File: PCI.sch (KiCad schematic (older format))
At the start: 67 parts

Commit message: workworkwork
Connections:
- net N12_PCI renamed N12V_PCI
- net P12_PCI renamed P12V_PCI
- removed net P3V3_PCI: C37.1, C38.1, C41.1, C42.1, C45.1, C46.1, C49.1, C50.1, PCI0.A10, PCI0.A16, PCI0.A21, PCI0.A27, PCI0.A33, PCI0.A39, PCI0.A45, PCI0.A53, PCI0.A59, PCI0.B19, PCI0.B25, PCI0.B31, PCI0.B36, PCI0.B41, PCI0.B43, PCI0.B54, PCI0.B59, PCI1.A10, PCI1.A16, PCI1.A21, PCI1.A27, PCI1.A33, PCI1.A39, PCI1.A45, PCI1.A53, PCI1.A59, PCI1.B19, PCI1.B25, PCI1.B31, PCI1.B36, PCI1.B41, PCI1.B43, PCI1.B54, PCI1.B59, PCI2.A10, PCI2.A16, PCI2.A21, PCI2.A27, PCI2.A33, PCI2.A39, PCI2.A45, PCI2.A53, PCI2.A59, PCI2.B19, PCI2.B25, PCI2.B31, PCI2.B36, PCI2.B41, PCI2.B43, PCI2.B54, PCI2.B59, PCI3.A10, PCI3.A16, PCI3.A21, PCI3.A27, PCI3.A33, PCI3.A39, PCI3.A45, PCI3.A53, PCI3.A59, PCI3.B19, PCI3.B25, PCI3.B31, PCI3.B36, PCI3.B41, PCI3.B43, PCI3.B54, PCI3.B59, R27.1, R28.1, R29.1, R30.1, R31.1, R32.1, R33.1, R34.1, R35.1, R36.1, R37.1, R38.1, R39.1, R40.1, R41.1, R42.1, R43.1, R44.1, R45.1, R46.1, R47.1, R48.1, R49.2
- net P3V3_PCI_AUX renamed P3V3_PCI_A
- net P3V3_PCI_A: now also C37.1, C38.1, C45.1, C46.1, PCI0.A10, PCI0.A16, PCI0.A21, PCI0.A27, PCI0.A33, PCI0.A39, PCI0.A45, PCI0.A53, PCI0.A59, PCI0.B19, PCI0.B25, PCI0.B31, PCI0.B36, PCI0.B41, PCI0.B43, PCI0.B54, PCI0.B59, PCI2.A10, PCI2.A16, PCI2.A21, PCI2.A27, PCI2.A33, PCI2.A39, PCI2.A45, PCI2.A53, PCI2.A59, PCI2.B19, PCI2.B25, PCI2.B31, PCI2.B36, PCI2.B41, PCI2.B43, PCI2.B54, PCI2.B59; no longer PCI1.A14, PCI3.A14
- net P5_PCI renamed P5V_PCI_A
- net P5V_PCI_A: no longer C40.1, C48.1, C72.1, C74.1, PCI1.A5, PCI1.A61, PCI1.A62, PCI1.A8, PCI1.B5, PCI1.B6, PCI1.B61, PCI1.B62, PCI3.A5, PCI3.A61, PCI3.A62, PCI3.A8, PCI3.B5, PCI3.B6, PCI3.B61, PCI3.B62
- new net P3V3_AUX: R39.1, R40.1, R41.1, R42.1, R43.1, R44.1, R45.1, R46.1, R47.1, R48.1, R49.2
- new net P3V3_BRIDGE: R27.1, R28.1, R29.1, R30.1, R31.1, R32.1, R33.1, R34.1, R35.1, R36.1, R37.1, R38.1
- new net P3V3_PCI_B: C41.1, C42.1, C49.1, C50.1, PCI1.A10, PCI1.A14, PCI1.A16, PCI1.A21, PCI1.A27, PCI1.A33, PCI1.A39, PCI1.A45, PCI1.A53, PCI1.A59, PCI1.B19, PCI1.B25, PCI1.B31, PCI1.B36, PCI1.B41, PCI1.B43, PCI1.B54, PCI1.B59, PCI3.A10, PCI3.A14, PCI3.A16, PCI3.A21, PCI3.A27, PCI3.A33, PCI3.A39, PCI3.A45, PCI3.A53, PCI3.A59, PCI3.B19, PCI3.B25, PCI3.B31, PCI3.B36, PCI3.B41, PCI3.B43, PCI3.B54, PCI3.B59
- new net P5V_PCI_B: C40.1, C48.1, C72.1, C74.1, PCI1.A5, PCI1.A61, PCI1.A62, PCI1.A8, PCI1.B5, PCI1.B6, PCI1.B61, PCI1.B62, PCI3.A5, PCI3.A61, PCI3.A62, PCI3.A8, PCI3.B5, PCI3.B6, PCI3.B61, PCI3.B62

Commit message: TODO: learn to write good commit messages
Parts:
- added C116, C117, C118, C119, C120, C121: 1u, IPC7351-Nominal:CAPC1005X55, symbol C-0402
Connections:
- net P3V3_BRIDGE: now also C116.2, C117.2, C118.2, C119.2, C120.2, C121.2
- net P3V3_PCI_A: now also C118.1, C120.1, C121.1
- net P3V3_PCI_B: now also C116.1, C117.1, C119.1

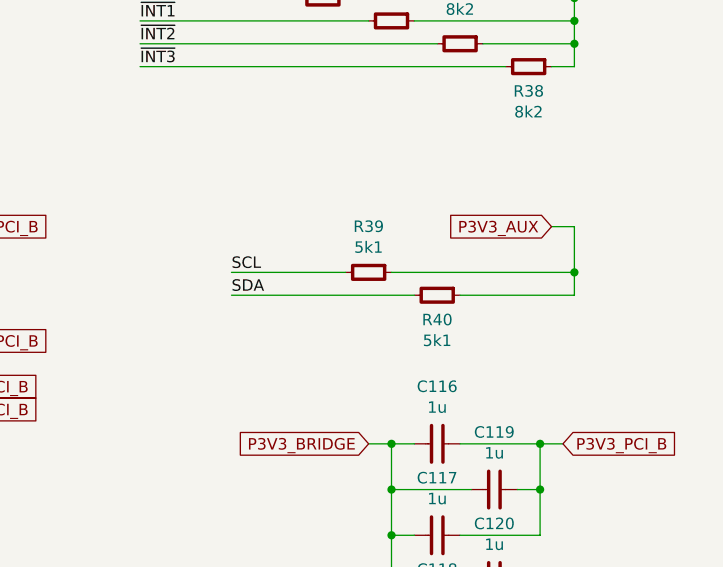
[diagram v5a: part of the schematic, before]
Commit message: Route PCI SMBUS
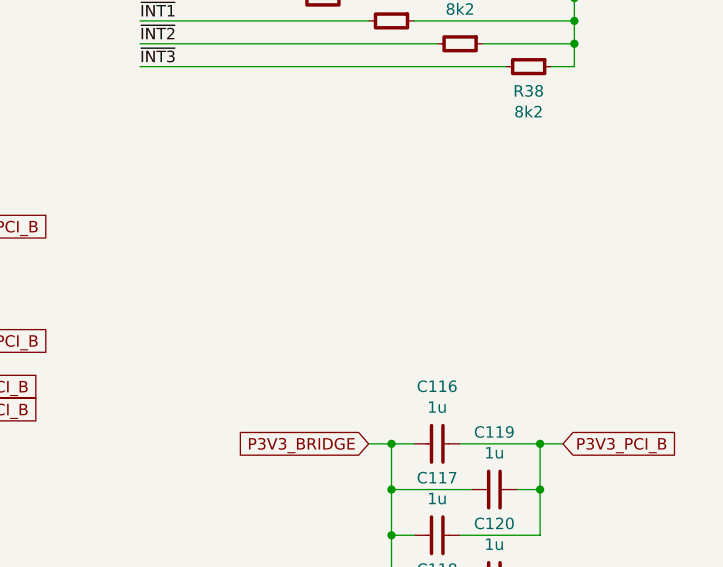
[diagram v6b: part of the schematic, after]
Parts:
- removed R39, R40: 5k1, IPC7351-Nominal:RESC1608X50, symbol R-0603
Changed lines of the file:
@@
-	0    1    1    0
-$EndComp
-$Comp
-L R-0603 R39
-U 1 1 576CDBBD
-P 14500 8200
-F 0 "R39" V 14300 8200 50  0000 C CNN
-F 1 "5k1" V 14391 8200 50  0000 C CNN
-F 2 "IPC7351-Nominal:RESC1608X50" H 14500 8200 50  0001 C CNN
-F 3 "" H 14500 8250 60  0000 C CNN
-F 4 "RES SMD 5k1 1% [0603]" H 15250 8750 60  0001 C CNN "BOM"
-	1    14500 8200
-	0    1    1    0
-$EndComp
-$Comp
-L R-0603 R40
-U 1 1 576CDF58
-P 14800 8300
-F 0 "R40" V 14908 8300 50  0000 C CNN
-F 1 "5k1" V 14999 8300 50  0000 C CNN
-F 2 "IPC7351-Nominal:RESC1608X50" H 14800 8300 50  0001 C CNN
-F 3 "" H 14800 8350 60  0000 C CNN
-F 4 "RES SMD 5k1 1% [0603]" H 15550 8850 60  0001 C CNN "BOM"
-	1    14800 8300
 	0    1    1    0
 $EndComp
@@
 Text Label 13500 6900 0    50   ~ 0
 ~LOCK
-Text Label 13900 8200 0    50   ~ 0
-SCL
-Text Label 13900 8300 0    50   ~ 0
-SDA
 Text Label 13700 2900 0    50   ~ 0
 M66EN
@@
 Text Notes 13400 3800 0    50   ~ 0
 Placement: Lo-Z: These capacitors provide\nAC return path for adjacent signals.
-Text GLabel 15300 8000 0    50   Input ~ 0
-P3V3_AUX
 $Comp
 L C-0402 C?
@@
 Wire Wire Line
 	11800 1300 14900 1300
-Connection ~ 15400 8200
-Wire Wire Line
-	14600 8200 15400 8200
-Wire Wire Line
-	15400 8300 14900 8300
-Wire Wire Line
-	15400 8000 15400 8300
-Wire Wire Line
-	15300 8000 15400 8000
-Wire Wire Line
-	13900 8300 14700 8300
-Wire Wire Line
-	14400 8200 13900 8200
 Connection ~ 15400 7200
 Wire Wire Line
